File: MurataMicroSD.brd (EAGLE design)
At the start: 25.6 x 12.8 mm, 12 parts, among them U1 IC_BLE_LBCA2HNZYZ-711

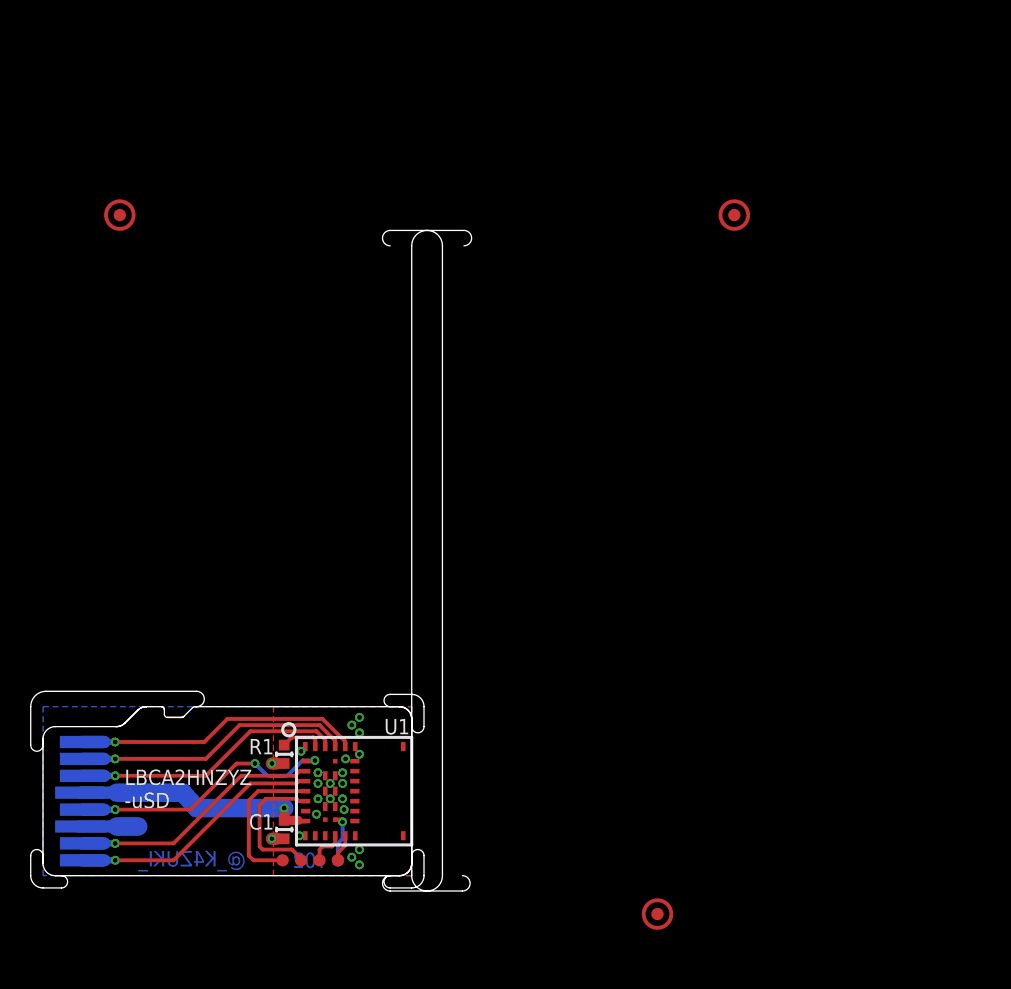
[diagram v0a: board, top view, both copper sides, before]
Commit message: [ uSD ][ FIX ] extend board size to 60x60
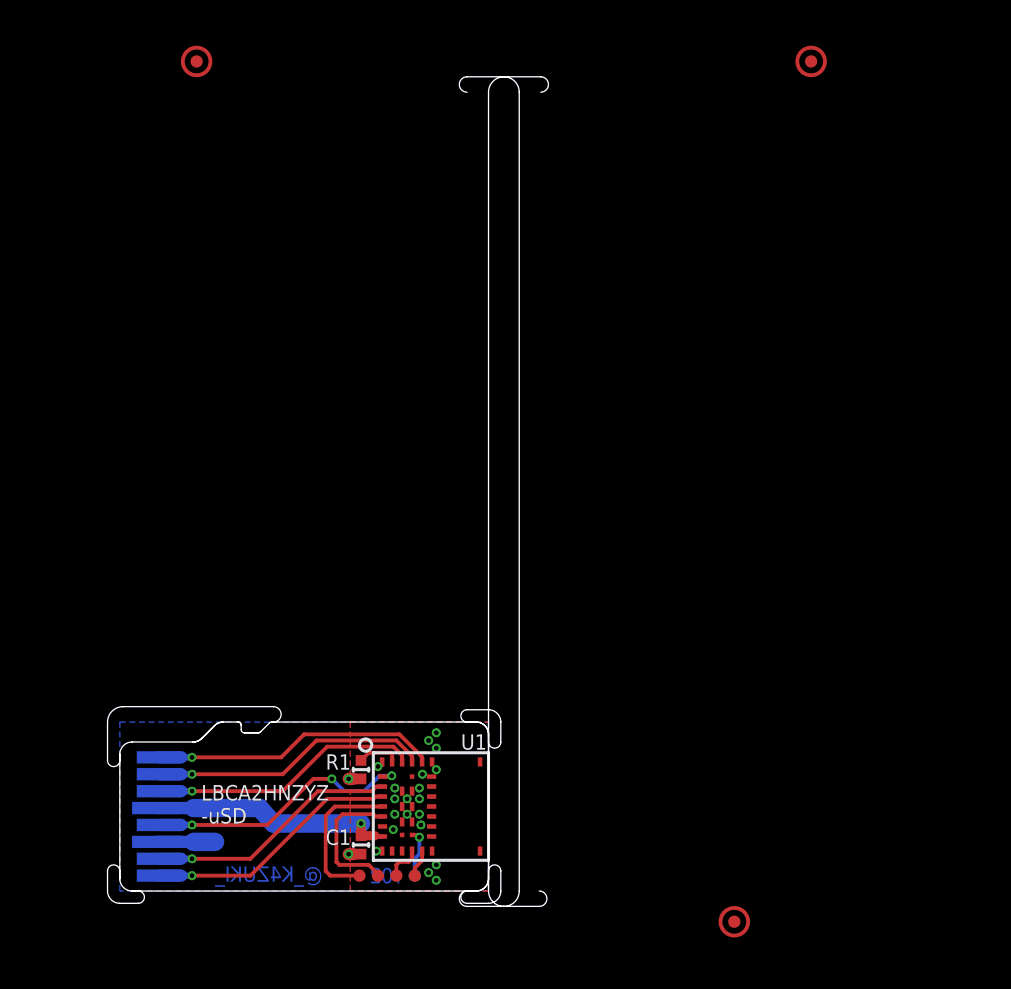
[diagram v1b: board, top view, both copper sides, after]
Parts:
- moved TP3 11.2 mm to (10.0, 58.0)
- moved TP5 11.2 mm to (50.0, 58.0)
- moved TP1 5.10 mm to (20.6, 5.00)
- moved C1 5.10 mm to (20.7, 7.00)
- moved C100 5.10 mm to (5.00, 15.0)
- moved R1 5.10 mm to (20.7, 11.9)
- moved TP2 5.10 mm to (21.8, 5.00)
- moved TP6 5.10 mm to (24.2, 5.00)
- moved TP7 5.10 mm to (23.0, 5.00)
- moved TP8 5.10 mm to (24.2, 5.00)
- moved U1 5.10 mm to (21.5, 13.0)
- moved TP4 5.02 mm to (45.0, 2.00)

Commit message: [ uSD ] fix as per library
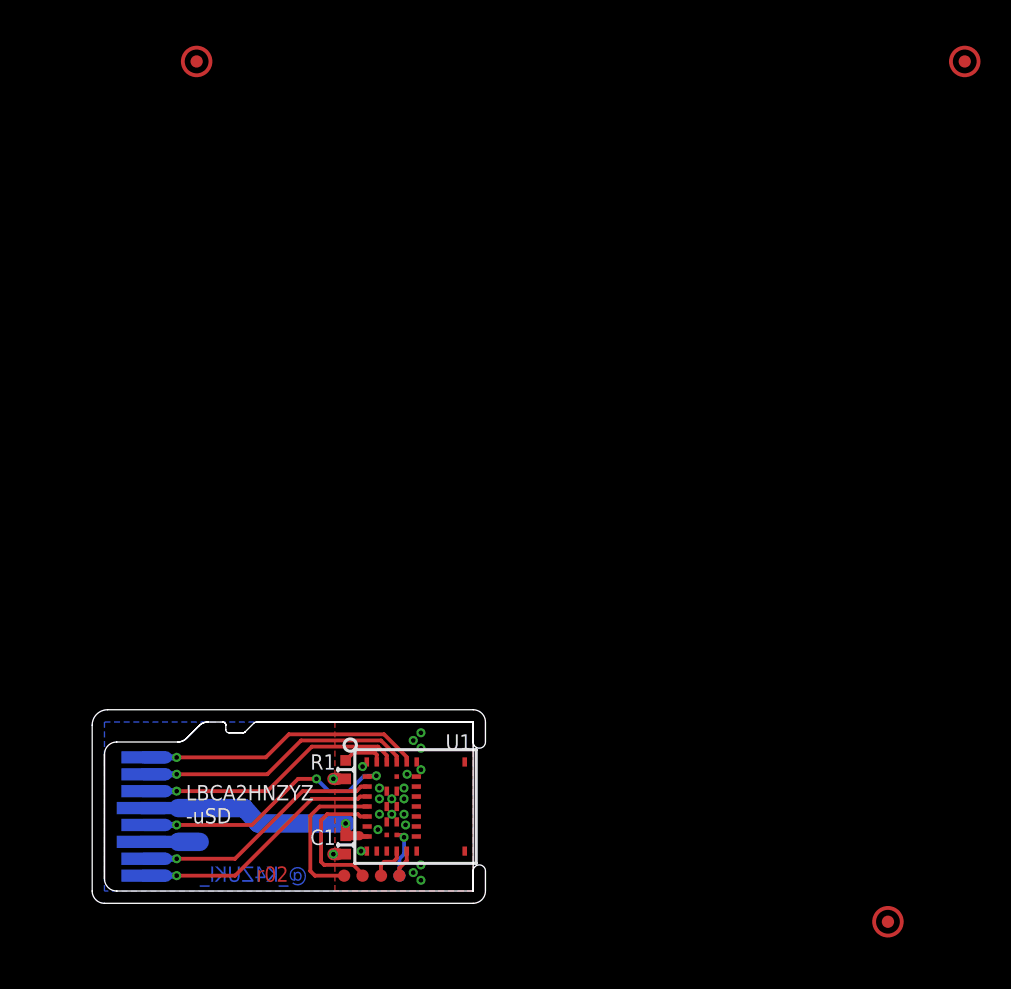
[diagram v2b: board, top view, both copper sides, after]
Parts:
- moved TP4 10.0 mm to (55.0, 2.00)
- moved TP5 10.0 mm to (60.0, 58.0)
- moved C1 1.00 mm to (19.7, 7.00)
- moved C100 1.00 mm to (4.00, 15.0)
- moved R1 1.00 mm to (19.7, 11.9)
- moved TP1 1.00 mm to (19.6, 5.00)
- moved TP2 1.00 mm to (20.8, 5.00)
- moved TP6 1.00 mm to (23.2, 5.00)
- moved TP7 1.00 mm to (22.0, 5.00)
- moved TP8 1.00 mm to (23.2, 5.00)
- moved U1 1.00 mm to (20.5, 13.0)
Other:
- board size 25.6 x 12.8 mm -> 25.6 x 12.6 mm

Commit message: [ uSD ] library update mylib.lbr: 324fe0c1e5958541035a4848493b76da56c91cd1
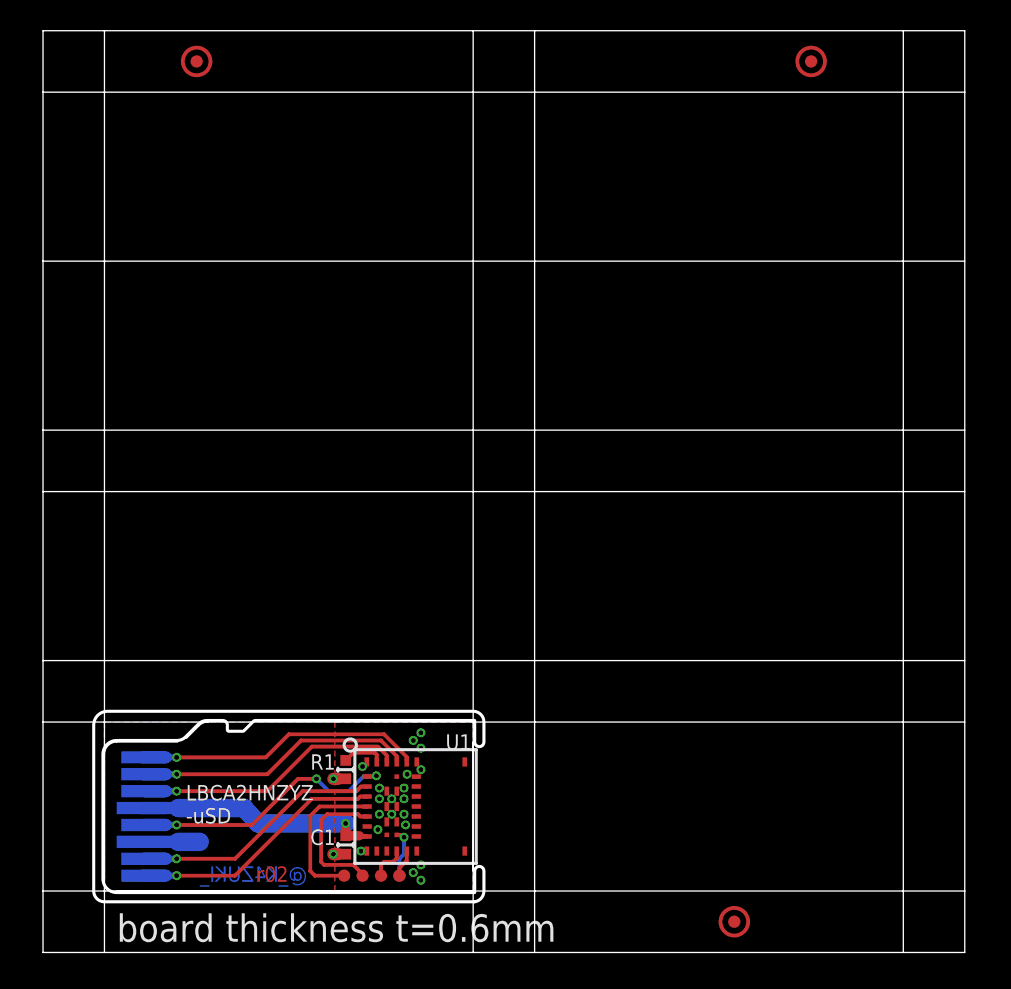
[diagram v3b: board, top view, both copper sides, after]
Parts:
- moved TP4 10.0 mm to (45.0, 2.00)
- moved TP5 10.0 mm to (50.0, 58.0)
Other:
- board size 25.6 x 12.6 mm -> 60 x 60 mm
- board text added: "board thickness t=0.6mm"
